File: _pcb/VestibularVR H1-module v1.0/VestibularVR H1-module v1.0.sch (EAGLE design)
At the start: 52 parts, among them IC1 FT232RL, IC2 74LVC1G07DBV, IC4 74LVC1G07DBV, IC5 74LVC1G07DBV, IC6 74LVC1G07DBV

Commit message: pcb v1.0 developed
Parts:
- removed C1: (no value), rcl:C-EUC0402
- removed F?, U$4: NDS332P, VestibularVR H1-module v1.0:NDS332P
- removed JP1: Lick_port_1, pinhead:PINHD-1X3
- removed JP10, JP9: Optical_flow_2, pinhead:PINHD-1X5
- removed JP2: Lick_port_2, pinhead:PINHD-1X3
- removed JP3: reward_valve_1, pinhead:PINHD-1X3
- removed JP4: reward_valve_2, pinhead:PINHD-1X3
- removed JP5: Camera_trigger_1, pinhead:PINHD-1X2
- removed JP6: Camera_trigger_2, pinhead:PINHD-1X2
- removed JP7: Optical_flow_1, pinhead:PINHD-1X7
- removed JP8: Optical_flow_2, pinhead:PINHD-1X7
- removed R4: (no value), rcl:R-US_R0402
- added J1: reward_valve_1, SparkFun-Connectors:CONN_03JST-PTH-VERT
- added J2: reward_valve_2, SparkFun-Connectors:CONN_03JST-PTH-VERT
- added J3: lick_port_1, SparkFun-Connectors:CONN_03JST-PTH-VERT
- added J4: lick_port_2, SparkFun-Connectors:CONN_03JST-PTH-VERT
- added J5: Optical_flow_1, SparkFun-Connectors:CONN_04X2
- added J6: Optical_flow_2, SparkFun-Connectors:CONN_04X2
- added J7: Camera_trigger_1, SparkFun-Connectors:CONN_02POLAR
- added J8: Camera_trigger_2, SparkFun-Connectors:CONN_02POLAR
- renumbered U$3 to IC9
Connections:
- removed net N$10: IC8.PA3/ADC3
- removed net N$11: IC8.PA2/ADC2
- removed net N$12: IC8.PA1/ADC1
- removed net N$13: IC8.PA0/ADC0/AREF
- removed net N$7: IC8.PA6/ADC6/AC1-OUT
- removed net N$8: IC8.PA5/ADC5
- new net LICK_PORT_1: IC6.A, J3.2
- new net LICK_PORT_2: IC5.A, J4.2
- new net U_LICK_PORT_1: IC6.Y, IC8.PA0/ADC0/AREF
- new net U_LICK_PORT_2: IC5.Y, IC8.PA1/ADC1
- new net U_REWARD_VALVE_1: IC8.PA6/ADC6/AC1-OUT, U$6.G
- new net U_REWARD_VALVE_2: IC8.PA7/ADC7/AC0-OUT, U$5.G
- net +3V3: now also J3.3, J4.3, J5.1, J6.1
- net +5V: now also D1.C, D2.C, J1.3, J2.3
- net GND: now also IC5.GND, IC6.GND, J3.1, J4.1, J5.7, J6.7, J7.1, J8.1, U$5.S, U$6.S; no longer JP5.2, JP6.2
- net N$16: now also IC2.Y, J7.2; no longer IC2.A, JP5.1
- net N$4: now also IC4.Y, J8.2; no longer IC4.A, JP6.1
- net N$6: now also D1.A, J2.1, U$5.D; no longer IC8.PA7/ADC7/AC0-OUT
- net N$9: now also D2.A, J1.1, U$6.D; no longer IC8.PA4/ADC4
- net U_CAM1_TRIGGER: now also IC2.A
- net U_CAM2_TRIGGER: now also IC4.A
- net U_OPTICAL_FLOW_1_CS: now also J5.2
- net U_OPTICAL_FLOW_1_INT: now also J5.5
- net U_OPTICAL_FLOW_1_MISO: now also J5.8
- net U_OPTICAL_FLOW_1_MOSI: now also J5.6
- net U_OPTICAL_FLOW_1_SCK: now also J5.4
- net U_OPTICAL_FLOW_2_CS: now also J6.2
- net U_OPTICAL_FLOW_2_INT: now also J6.5
- net U_OPTICAL_FLOW_2_MISO: now also J6.8
- net U_OPTICAL_FLOW_2_MOSI: now also J6.6
- net U_OPTICAL_FLOW_2_SCK: now also J6.4
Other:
- note added: "level shifter!! ?"
- note added: "sensor to new photodiode get to know mouse tongue on water >> decide photodiode PN !!!"
- note removed: "level shifter!!"
- note removed: "sensor to new photodiode know mouse tongue on water >> decide photodiode PN !!!"
- moved on the sheet: D1, D2, IC2, IC4, IC5, IC6, R1, R2, R5, R6, U$5, U$6

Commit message: proceeding design VestibularVR H1
- Eagle version changed back to v.8.3.1
- proceeding design VestibularVR H1-module v1.0
- added Lick Sensor module v1.0
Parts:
- removed D2: BZX84CSMD, diode:BZX84CSMD
- removed IC9: USBLC6-2SC6, VestibularVR H1-module v1.0:USBLC6-2SC6
- removed J1: reward_valve_1, SparkFun-Connectors:CONN_03JST-PTH-VERT
- removed J2: reward_valve_2, SparkFun-Connectors:CONN_03JST-PTH-VERT
- removed J3: lick_port_1, SparkFun-Connectors:CONN_03JST-PTH-VERT
- removed J4: lick_port_2, SparkFun-Connectors:CONN_03JST-PTH-VERT
- removed J7: Camera_trigger_1, SparkFun-Connectors:CONN_02POLAR
- removed J8: Camera_trigger_2, SparkFun-Connectors:CONN_02POLAR
- removed OSC1: OSCILLATOR, harp camera controller:OSCILLATOR
- added C10, C11: 4.7uF, rcl:C-EUC0603
- added C12: 100nF, rcl:C-EUC0402
- added CAMERA_TRIGGER_1, CAMERA_TRIGGER_2, REWARD_VALVE_1, REWARD_VALVE_2: 22-23-2021, con-molex:22-23-2021
- added D4: BAT54, diode:BAT54
- added IC3: TLV70033DDCR, VestibularVR H1-module v1.0:TLV700XX
- added IC7: USBLC6-2SC6, VestibularVR H1-module v1.0:USBLC6-2SC6
- added LICK_PORT_1, LICK_PORT_2: 22-23-2031, con-molex:22-23-2031
- added R4, R7: 10k, rcl:R-US_R0402
- added U$2: OSCILLATOR, VestibularVR H1-module v1.0:OSCILLATOR
- added X7: 22-23-2051, con-molex:22-23-2051
- C8: device rcl:CPOL-EUA/3216-18W -> rcl:CPOL-EUA/3216-18R
- D1: value BZX84CSMD -> BAT54; device diode:BZX84CSMD -> diode:BAT54
- F1: device harp camera controller:BLM15HF0603 -> VestibularVR H1-module v1.0:BLM15HF0603
- IC8: value (none) -> ATXMEGA32A4U
- R18, R34: device rcl:R-EU_R0402 -> rcl:R-US_R0402
- SV2: value (none) -> PINHD-2X3; device con-lstb:MA03-2 -> Connector:PINHD-2X3
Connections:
- removed net N$15: C5.1, C8.+, IC1.VCC, L1.1
- removed net U_HARP_H1_BOARD_RX: IC8.OC0C/RXD0/PD2
- removed net U_HARP_H1_BOARD_TX: IC8.OC0D/TXD0/PD3
- removed net VDD: C25.1, C26.1, C27.1, C28.1, C29.1, C30.1, F1.1, IC8.AVCC, IC8.VCC@1, IC8.VCC@2, IC8.VCC@3, OSC1.VDD, R34.2, SV2.6
- new net +12V: X7-5.S
- new net +3V3_U: C25.1, C26.1, C27.1, C28.1, C29.1, C30.1, F1.1, IC8.AVCC, IC8.VCC@1, IC8.VCC@2, IC8.VCC@3, R34.2, SV2.6, U$2.VDD
- new net HARP_H1_BOARD_RX: IC8.OC0C/RXD0/PD2, X7-3.S
- new net HARP_H1_BOARD_TX: IC8.OC0D/TXD0/PD3, X7-4.S
- new net HARP_H1_CLOCK_IN: IC8.PC2/OC0C/RXD0, X7-2.S
- new net N$7: D4.C, REWARD_VALVE_2-2.S
- new net N$8: D1.C, REWARD_VALVE_1-2.S
- net +3V3: now also C11.1, C12.1, IC3.OUT, IC5.VCC, IC6.VCC, LICK_PORT_1-3.S, LICK_PORT_2-3.S; no longer J3.3, J4.3
- net +5V: now also C10.1, C5.1, C8.+, IC1.VCC, IC3.EN, IC3.IN, L1.1; no longer D1.C, D2.C, J1.3, J2.3
- net GND: now also C10.2, C11.2, C12.2, CAMERA_TRIGGER_1-1.S, CAMERA_TRIGGER_2-1.S, IC3.GND, IC7.GND, LICK_PORT_1-1.S, LICK_PORT_2-1.S, R4.1, R7.1, U$2.GND, X7-1.S; no longer IC9.GND, J3.1, J4.1, J7.1, J8.1, OSC1.GND
- net LICK_PORT_1: now also LICK_PORT_1-2.S; no longer J3.2
- net LICK_PORT_2: now also LICK_PORT_2-2.S; no longer J4.2
- net N$16: now also CAMERA_TRIGGER_1-2.S; no longer J7.2
- net N$2: now also IC7.IO2@1; no longer IC9.IO1@1
- net N$3: now also IC7.IO1@1; no longer IC9.IO2@1
- net N$4: now also CAMERA_TRIGGER_2-2.S; no longer J8.2
- net N$6: now also D4.A, REWARD_VALVE_2-1.S; no longer D1.A, J2.1
- net N$9: now also D1.A, REWARD_VALVE_1-1.S; no longer D2.A, J1.1
- net OSC2: now also U$2.OUTPUT; no longer OSC1.OUTPUT
- net USBDM: now also IC7.IO1@0; no longer IC9.IO2@0
- net USBDP: now also IC7.IO2@0; no longer IC9.IO1@0
- net USB_POWER: now also IC7.VBUS; no longer IC9.VBUS
- net U_CAM2_TRIGGER: now also IC8.OC0A/PD0; no longer IC8.PB1/ADC9
- net U_OPTICAL_FLOW_1_INT: no longer IC8.OC0A/PD0
- net U_OPTICAL_FLOW_2_INT: no longer IC8.OC0B/XCK0/PD1
- net U_REWARD_VALVE_1: now also R4.2
- net U_REWARD_VALVE_2: now also R7.2
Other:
- note added: "Camera_trigger_1"
- note added: "Camera_trigger_2"
- note added: "PAA5100JE Optical tracking - can be powered @ 3V3 oe 5V - line outputs level will depend of power"
- note added: "check CTS RTS to E0 and E1 port verificado com cammera controller - OK"
- note added: "lick sensor @3V3 GP1A57HRJ00F photointerrupter - design from FED3"
- note added: "lick_port_1"
- note added: "lick_port_2"
- note added: "main plug"
- note added: "reward_valve_1"
- note added: "reward_valve_2"
- note removed: "Vcc FTDI tb a net +5V ??"
- note removed: "check CTS RTS to E0 and E1 port"
- note removed: "level shifter!! ?"
- note removed: "sensor to new photodiode get to know mouse tongue on water >> decide photodiode PN !!!"
- moved on the sheet: C2, C25, C26, C27, C28, C29, C3, C30, C37, C4, C5, C6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

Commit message: update on VestibularVR & LickSensor
- returned to Eagle 9.6.2
- projects reviewed with Filipe
- LickSensor board with reviews already made
- VestibularVR  board starting implementing reviews
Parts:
- removed C30, C37: 330pF, rcl:C-EUC0402
- removed F1: 330 Ohms @ 100MHz, VestibularVR H1-module v1.0:BLM15HF0603
- removed REWARD_VALVE_1, REWARD_VALVE_2: 22-23-2021, con-molex:22-23-2021
- added C1, C14, C15, C16: 100nF, rcl:C-EUC0402
- added C13: 47pF, rcl:C-EUC0402
- added L2: 40R@100MHz, rcl:R-EU_R0805
- added R8, R9: 10k, rcl:R-US_R0402
- added VALVE_1, VALVE_2: 22-23-2021, con-molex:22-23-2021
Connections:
- removed net N$8: D1.C, REWARD_VALVE_1-2.S
- removed net U_HARPH1CLOCKIN: IC8.PB3/ADC11/DAC1
- net +12V: now also D1.C, VALVE_1-2.S
- net +3V3: now also L2.2; no longer F1.2
- net +3V3_U: now also C1.1, L2.1; no longer C30.1, F1.1
- net GND: now also C1.2, C13.2, R8.1, R9.1; no longer C30.2, C37.2
- net LICK_PORT_1: now also R9.2
- net LICK_PORT_2: now also R8.2
- net N$6: now also VALVE_2-1.S; no longer REWARD_VALVE_2-1.S
- net N$7: now also VALVE_2-2.S; no longer REWARD_VALVE_2-2.S
- net N$9: now also VALVE_1-1.S; no longer REWARD_VALVE_1-1.S
- net PDI_CLK: now also C13.1; no longer C37.1
- net U_CAM1_TRIGGER: now also IC8.PC0/OC0A/SDA; no longer IC8.PB0/ADC8/AREF
- net U_OPTICAL_FLOW_1_INT: now also IC8.PB0/ADC8/AREF
- net U_OPTICAL_FLOW_2_CS: no longer IC8.PC4/OC1A/!SS
- net U_OPTICAL_FLOW_2_INT: now also IC8.PB1/ADC9
- net U_OPTICAL_FLOW_2_MISO: no longer IC8.PC6/MISO/RXD1
- net U_OPTICAL_FLOW_2_MOSI: no longer IC8.PC5/OC1B/MOSI/XCK1
- net U_OPTICAL_FLOW_2_SCK: no longer IC8.PC7/SCK/TXD1/CLKO/EVO
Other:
- note added: "Cammera Triggers"
- note added: "Lick Ports"
- note added: "Main Plug"
- note added: "Optical Flows"
- note added: "Reward Valves"
- note added: "a reverificar: - pinos CTS RTS: correctos com refª q o Filipe disse? - u_CAM_x trigger em pinos PD0 & PB0; interrupts level; Certo? - HARP_HQ_CLOCK_IN em PC": OK? - u_OPTICAL_FLOW_1_INT: verificar os pinos"
- note added: "passar 1x4"
- note removed: "check CTS RTS to E0 and E1 port verificado com cammera controller - OK"
- note removed: "main plug"
- moved on the sheet: C10, C11, C12, C2, C25, C26, C27, C28, C29, C3, C4, C5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

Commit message: VestibularVR H1-module v1.0 - revisions made with Filipe updated
Revisions made:
- added missing decoupler caps
- considered components on top & bottom side
- review pinout on micro

Next steps:
- final mechanical integration
- final plugs choose
.. and.. something more??
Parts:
- removed CAMERA_TRIGGER_1, CAMERA_TRIGGER_2: 22-23-2021, con-molex:22-23-2021
- added C17: 100nF, rcl:C-EUC0402
- added CAMM_TRIGGER: 22-23-2041, con-molex:22-23-2041
- added J1: (no value), SparkFun-Connectors:CONN_05X2SHD
- added J3: (no value), SparkFun-Connectors:CONN_05X2PTH
- added TP1, TP10, TP11, TP12: WIREPADSMD1,27-254, wirepad:SMD2
- added TP2, TP3, TP4, TP5, TP6, TP7, TP8, TP9: WIREPADSMD1,27-254, testpad:TPSQTP11R
- added X1: TSW-105-02-S-D, con-samtec:TSW-105-02-S-D
- J5: device SparkFun-Connectors:CONN_04X2 -> SparkFun-Connectors:CONN_05X2SHD_LOCK
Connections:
- new net N$10: IC8.PA3/ADC3, TP3.TP
- new net N$11: IC8.PA4/ADC4, TP4.TP
- new net N$12: IC8.PA5/ADC5, TP5.TP
- new net N$13: IC8.PB2/ADC10/DAC0, TP6.TP
- new net N$15: IC8.PB3/ADC11/DAC1, TP7.TP
- new net N$17: IC8.PC1/OC0B/XCK0/SCL, TP8.TP
- new net N$18: IC8.OC0B/XCK0/PD1, TP9.TP
- new net N$8: IC8.PA2/ADC2, TP2.TP
- net +3V3: now also C14.1, C17.1, TP1.P
- net +5V: now also TP10.P
- net GND: now also C14.2, C15.2, C16.2, C17.2, CAMM_TRIGGER-1.S, CAMM_TRIGGER-3.S, TP11.P, TP12.P; no longer CAMERA_TRIGGER_1-1.S, CAMERA_TRIGGER_2-1.S
- net N$14: now also C15.1
- net N$16: now also CAMM_TRIGGER-4.S; no longer CAMERA_TRIGGER_1-2.S
- net N$4: now also CAMM_TRIGGER-2.S; no longer CAMERA_TRIGGER_2-2.S
- net N$5: now also C16.1
- net U_OPTICAL_FLOW_1_CS: now also IC8.PC4/OC1A/!SS; no longer IC8.OC1A/!SS!/PD4
- net U_OPTICAL_FLOW_1_MISO: now also IC8.PC6/MISO/RXD1; no longer IC8.D-/RXD1/MISO/PD6
- net U_OPTICAL_FLOW_1_MOSI: now also IC8.PC5/OC1B/MOSI/XCK1; no longer IC8.OCB1/XCK1/MOSI/PD5
- net U_OPTICAL_FLOW_1_SCK: now also IC8.PC7/SCK/TXD1/CLKO/EVO; no longer IC8.D+/TXD1/SCK/PD7
- net U_OPTICAL_FLOW_2_CS: now also IC8.OC1A/!SS!/PD4
- net U_OPTICAL_FLOW_2_MISO: now also IC8.D-/RXD1/MISO/PD6
- net U_OPTICAL_FLOW_2_MOSI: now also IC8.OCB1/XCK1/MOSI/PD5
- net U_OPTICAL_FLOW_2_SCK: now also IC8.D+/TXD1/SCK/PD7
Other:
- note added: "Camera_trigger 1 & 2"
- note removed: "Camera_trigger_1"
- note removed: "Camera_trigger_2"
- moved on the sheet: C14, C15, C16, IC5, IC6, LICK_PORT_1-1, LICK_PORT_1-2, LICK_PORT_1-3, R9

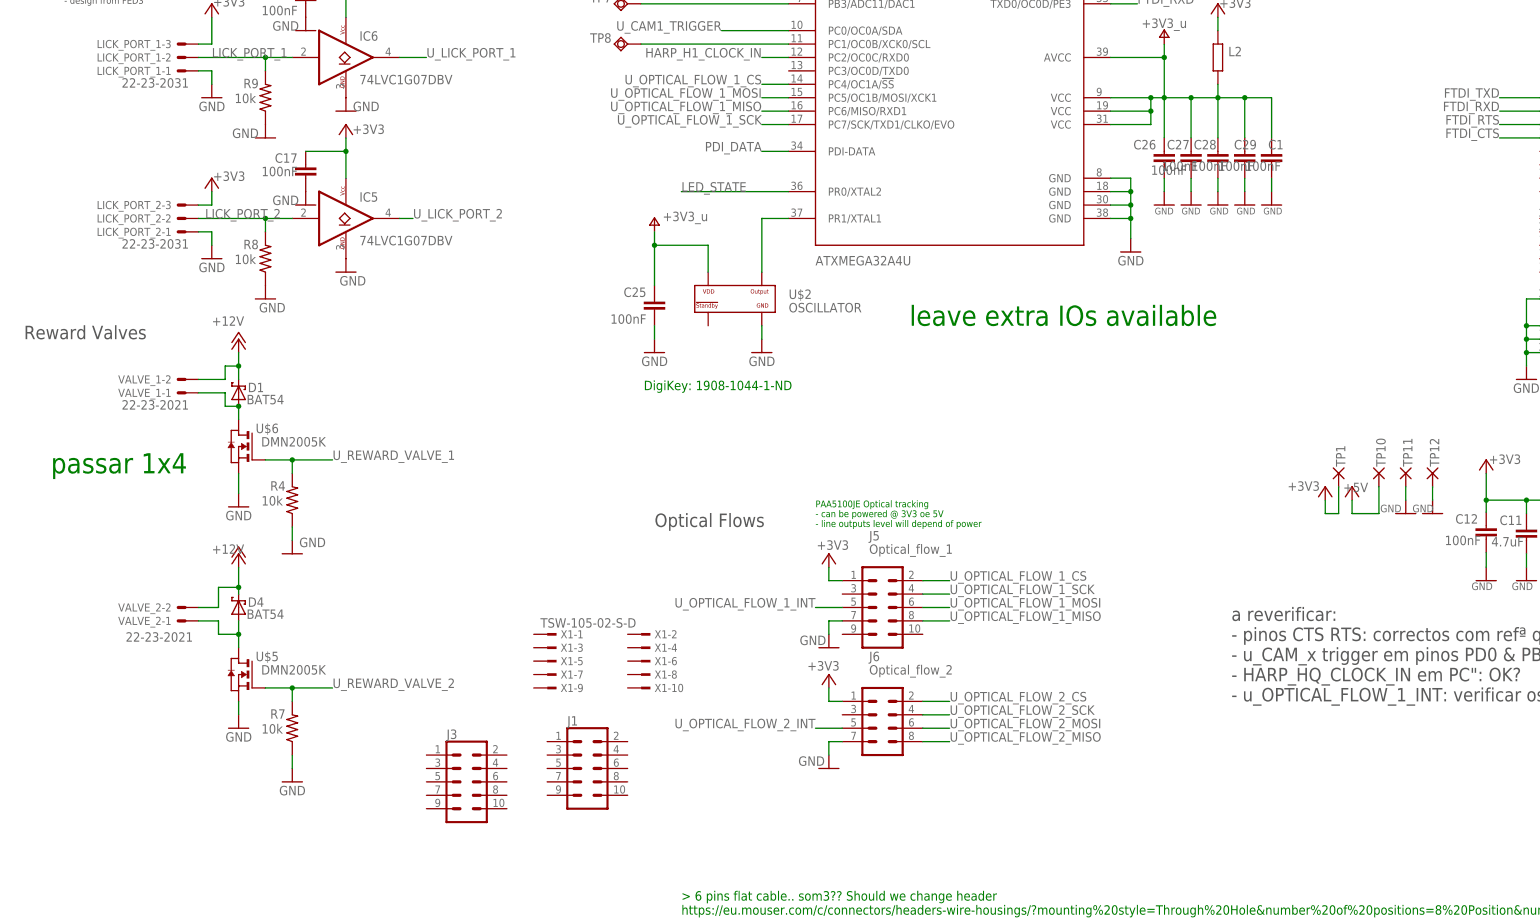
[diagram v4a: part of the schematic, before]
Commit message: . schm design reviewed 2nd time with Filipe . pcb design already started; not finished
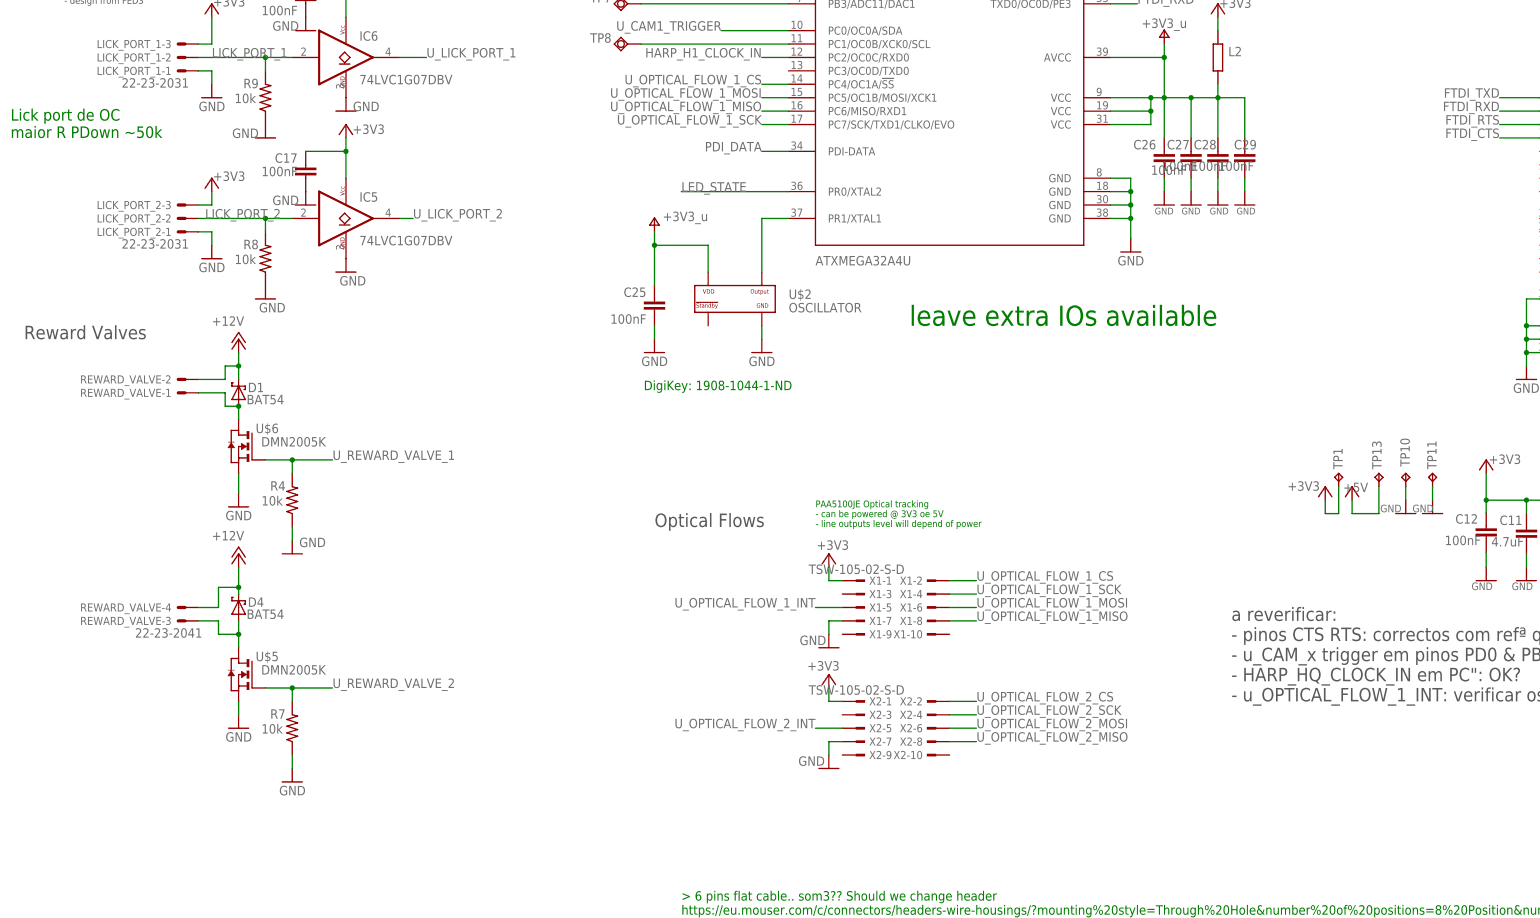
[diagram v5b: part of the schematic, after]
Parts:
- removed C1: 100nF, rcl:C-EUC0402
- removed J1: (no value), SparkFun-Connectors:CONN_05X2SHD
- removed J3: (no value), SparkFun-Connectors:CONN_05X2PTH
- removed J5: Optical_flow_1, SparkFun-Connectors:CONN_05X2SHD_LOCK
- removed J6: Optical_flow_2, SparkFun-Connectors:CONN_04X2
- removed TP12: WIREPADSMD1,27-254, wirepad:SMD2
- removed VALVE_1, VALVE_2: 22-23-2021, con-molex:22-23-2021
- added REWARD_VALVE: 22-23-2041, con-molex:22-23-2041
- added TP13: TPB1,27, testpad:TPB1,27
- added X2: TSW-105-02-S-D, con-samtec:TSW-105-02-S-D
- C10, C11: device rcl:C-EUC0603 -> rcl:C-EUC0603K
- C12, C13, C14, C15, C16, C17, C2, C25, C26, C27, C28, C29, C4, C5, C6, C7: device rcl:C-EUC0402 -> rcl:C-EUC0402K
- TP1, TP10, TP11: value WIREPADSMD1,27-254 -> TPB1,27; device wirepad:SMD2 -> testpad:TPB1,27
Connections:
- removed net N$9: D1.A, U$6.D, VALVE_1-1.S
- net +12V: now also D4.C, REWARD_VALVE-2.S, REWARD_VALVE-4.S; no longer VALVE_1-2.S
- net +3V3: now also TP1.TP, X1-1.1, X2-1.1; no longer J5.1, J6.1, TP1.P
- net +3V3_U: no longer C1.1
- net +5V: now also TP13.TP; no longer TP10.P
- net GND: now also TP10.TP, TP11.TP, X1-7.1, X2-7.1; no longer C1.2, J5.7, J6.7, TP11.P, TP12.P
- net N$6: now also REWARD_VALVE-3.S; no longer VALVE_2-1.S
- net N$7: now also D1.A, REWARD_VALVE-1.S, U$6.D; no longer D4.C, VALVE_2-2.S
- net U_OPTICAL_FLOW_1_CS: now also X1-2.1; no longer J5.2
- net U_OPTICAL_FLOW_1_INT: now also X1-5.1; no longer J5.5
- net U_OPTICAL_FLOW_1_MISO: now also X1-8.1; no longer J5.8
- net U_OPTICAL_FLOW_1_MOSI: now also X1-6.1; no longer J5.6
- net U_OPTICAL_FLOW_1_SCK: now also X1-4.1; no longer J5.4
- net U_OPTICAL_FLOW_2_CS: now also X2-2.1; no longer J6.2
- net U_OPTICAL_FLOW_2_INT: now also X2-5.1; no longer J6.5
- net U_OPTICAL_FLOW_2_MISO: now also X2-8.1; no longer J6.8
- net U_OPTICAL_FLOW_2_MOSI: now also X2-6.1; no longer J6.6
- net U_OPTICAL_FLOW_2_SCK: now also X2-4.1; no longer J6.4
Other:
- note added: "Lick port de OC maior R PDown ~50k"
- note removed: "passar 1x4"
- moved on the sheet: X1-1, X1-10, X1-2, X1-3, X1-4, X1-5, X1-6, X1-7, X1-8, X1-9

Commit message: . pcb design; not finnished
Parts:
- added R10: 910, rcl:R-EU_R0402
- added STATE: (no value), led:LEDCHIP-LED0603
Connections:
- new net N$9: R10.2, STATE.C
- net GND: now also R10.1
- net LED_STATE: now also STATE.A
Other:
- moved on the sheet: C10, C11, C12, IC3, TP1, TP10, TP11, TP13, X1-1, X1-10, X1-2, X1-3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
